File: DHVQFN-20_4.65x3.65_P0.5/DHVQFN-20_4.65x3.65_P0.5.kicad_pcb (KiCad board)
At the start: 2 copper layers, 20.3 x 30.5 mm, 6 parts, among them J101 Conn_01x12, J102 Conn_01x12, J103 Conn_01x12, J104 Conn_01x12, U101 QFN-20

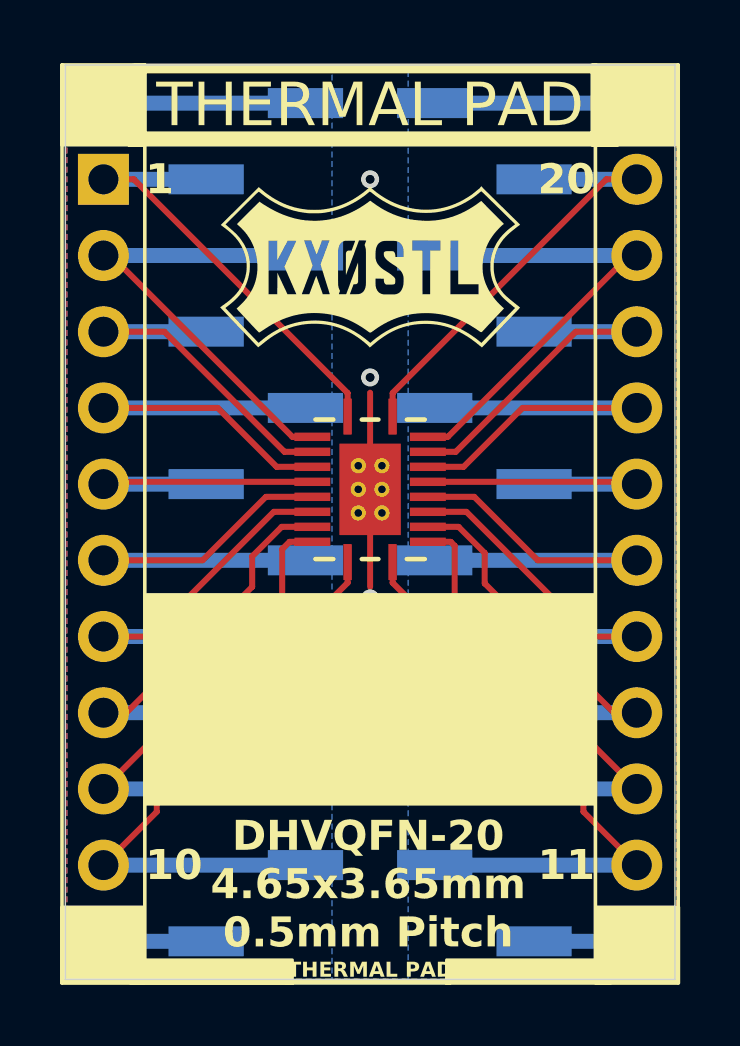
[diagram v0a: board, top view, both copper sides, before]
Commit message: Created SMDIP-16, QFP-48, QFP-32, QFN-80, QFN-68, QFN-64, QFN-60, QFN-56, QFN-48, QFN-36, QFN-28, QFN-20, QFP-32, QFP-48
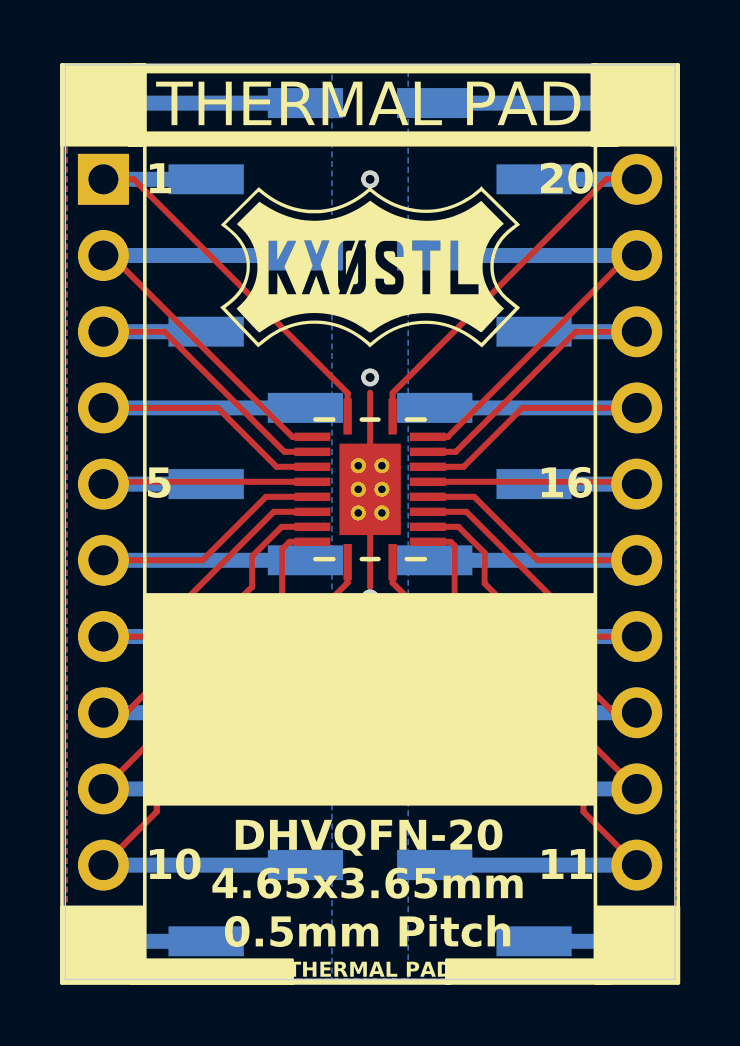
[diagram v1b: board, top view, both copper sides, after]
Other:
- board text added: "16"
- board text added: "5"
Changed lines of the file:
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@@
 		(layer "Edge.Cuts")
+	)
+	(gr_text "16"
+		(at 145.906 119.36 0)
+		(layer "F.SilkS")
+		(effects
+			(font
+				(size 1 1)
+				(thickness 0.2)
+				(bold yes)
+			)
+			(justify right)
+		)
 	)
 	(gr_text "20"
@@
 		)
 	)
+	(gr_text "5"
+		(at 130.92 119.36 0)
+		(layer "F.SilkS")
+		(effects
+			(font
+				(size 1 1)
+				(thickness 0.2)
+				(bold yes)
+			)
+			(justify left)
+		)
+	)
